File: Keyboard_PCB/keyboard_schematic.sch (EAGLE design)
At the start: 260 parts, among them M2 KEYSWITCH-RGBSMDLED-ALPSMX-1U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, M3 KEYSWITCH-RGBSMDLED-ALPSMX-1U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, M4 KEYSWITCH-RGBSMDLED-ALPSMX-1U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, M5 KEYSWITCH-RGBSMDLED-ALPSMX-1U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, M6 KEYSWITCH-RGBSMDLED-ALPSMX-1U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, Y2 CRYSTAL-GROUNDEDSMD-3.2X2.5

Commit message: Changed MCU to a larger chip
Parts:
- removed J1: (no value), SparkFun-Connectors:USB_MICRO-B_FEMALE-SMT
- removed U$1: 32U4, SparkFun-IC-Microcontroller:ATMEGA32U4TQFP-44
- added IC1: LMV321M5, linear:LMV321M5
- added IC2: (no value), controller-micro_atmel_jd:AT90USB-QFN
- added R5, R6: 5.1k, rcl:R-US_M0805
- added R7: 475, rcl:R-US_M0805
- added R8: 150, rcl:R-US_M0805
- added T1: BC846, transistor:BC846
- added U$2: PCB_USB_CDS_1, USB_pcb_connectors:PCB_USB_CDS_1
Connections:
- new net +5V: IC1.V+, IC2.AREF, IC2.AVCC, IC2.VCC, IC2.VCC@1, R7.2, T1.C, U$2.A4, U$2.A9, U$2.B4, U$2.B9
- new net CC1: R5.1, U$2.A5
- new net CC2: IC1.+IN, R6.2, U$2.B5
- new net LED_VCC: T1.E
- new net N$116: IC1.-IN, R7.1, R8.2
- new net N$117: IC1.OUT, T1.B
- net COL1: no longer U$1.PF7(ADC7)
- net COL10: no longer U$1.PC6
- net COL11: no longer U$1.PD7(ADC10)
- net COL12: no longer U$1.PE6
- net COL2: no longer U$1.PF6(ADC6)
- net COL3: no longer U$1.PF5(ADC5)
- net COL4: no longer U$1.PF4(ADC4)
- net COL5: no longer U$1.PF1(ADC1)
- net COL6: no longer U$1.PF0(ADC0)
- net COL7: no longer U$1.PD1(SDA)
- net COL8: no longer U$1.PD0(SCL)
- net COL9: no longer U$1.PD4(ADC8)
- net D+32U: now also IC2.D+; no longer U$1.D+
- net D+USB: now also U$2.A6; no longer J1.D+
- net D-32U4: now also IC2.D-; no longer U$1.D-
- net D-USB: now also U$2.A7; no longer J1.D-
- net GND: now also IC1.V-, IC2.AGND, IC2.GND, IC2.GND@1, IC2.UGND, R5.2, R6.1, R8.1, U$2.A1, U$2.A12, U$2.B1, U$2.B12; no longer J1.GND, J1.SHIELD, U$1.GND@15, U$1.GND@23, U$1.GND@35, U$1.GND@43, U$1.UGND
- net PE2: now also IC2.PE2_ALE_HWB; no longer U$1.PE2/!HWB
- net RESET: now also IC2./RESET; no longer U$1.!RESET
- net ROW1.1: no longer U$1.PB4(ADC11)
- net ROW1.2: no longer U$1.PB5(ADC12)
- net ROW2.1: no longer U$1.PB6(ADC13)
- net ROW2.2: no longer U$1.PB7
- net ROW3.1: no longer U$1.PD6(ADC9)
- net ROW3.2: no longer U$1.PC7
- net ROW4.1: no longer U$1.PB0(SS)
- net ROW4.2: no longer U$1.PB1(SCK)
- net ROW5.1: no longer U$1.PB2(MOSI)
- net ROW5.2: no longer U$1.PB3(MISO)
- net ROW6.1: no longer U$1.PD5
- net UCAP: now also IC2.UCAP; no longer U$1.UCAP
- net VCC: no longer J1.VBUS, U$1.AVCC@24, U$1.AVCC@44, U$1.UVCC, U$1.VCC@14, U$1.VCC@34
- net XTAL1: now also IC2.XTAL1; no longer U$1.XTAL1
- net XTAL2: now also IC2.XTAL2; no longer U$1.XTAL2

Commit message: Updated Schematics and boards
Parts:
- removed IC2: (no value), controller-micro_atmel_jd:AT90USB-QFN
- removed U$2: PCB_USB_CDS_1, USB_pcb_connectors:PCB_USB_CDS_1
- added IC3: (no value), controller-micro_atmel_jd:AT90USB-TQFP
- added J1: 1-2295018-2, 1-2295018-2:1-2295018-2
- T1: value BC846 -> (none); device transistor:BC846 -> transistor:-NPN-SOT23-EBC
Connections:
- removed net COL11: EQUAL2.P0, KP_9.P0, KP_ASTERISK.P0, KP_DASH.P0, NEXTSONG.P0, PAUSEPLAY.P0
- removed net ROW1.1: DF1.C, DF11.C, DF3.C, DF5.C, DF7.C, DF9.C, DM6.C, DNEXTSONG1.C, DPAUSE.C, DPAUSEPLAY.C, DSCROLLLOCK.C, DVOLUMEUP.C
- removed net ROW1.2: DBACKSONG.C, DESC.C, DF10.C, DF12.C, DF2.C, DF4.C, DF6.C, DF8.C, DLOCK.C, DNEXTSONG.C, DPRTSC.C, DVOLUMNEDOWN.C
- removed net ROW2.1: D1.C, D3.C, D5.C, D7.C, D9.C, DBACKSPACE.C, DDASH.C, DHOME.C, DKP_DASH.C, DKP_SLASH.C, DM5.C
- removed net ROW2.2: D0.C, D2.C, D4.C, D6.C, D8.C, DEQUAL.C, DGRAVE.C, DINSERT.C, DKP_ASTERISK.C, DNUMLOCK.C, DPGUP.C, DUNDERSCORE.C
- removed net ROW3.1: DBACKSLASH.C, DE.C, DEND.C, DEQUAL2.C, DKP_8.C, DLBRACKET.C, DM4.C, DO.C, DQ.C, DT.C, DU.C
- removed net ROW3.2: DDELETE.C, DI.C, DKP_5.C, DKP_7.C, DKP_9.C, DP.C, DPGDN.C, DR.C, DRBRACKET.C, DTAB.C, DW.C, DY.C
- removed net ROW4.1: DA.C, DCTRL2.C, DD.C, DG.C, DJ.C, DKP_4.C, DKP_6.C, DKP_62.C, DL.C, DM3.C, DQUOTE.C
- removed net ROW4.2: DCAPSLOCK.C, DENTER.C, DENTER2.C, DF.C, DH.C, DK.C, DKP_52.C, DS.C, DSEMICOLON.C, DUP.C
- removed net ROW5.1: DB.C, DC.C, DKP_2.C, DLEFT.C, DM.C, DM2.C, DMENU.C, DPERIOD.C, DZ.C
- removed net ROW5.2: DCOMMA.C, DDELETE2.C, DKP_1.C, DKP_3.C, DN.C, DRIGHT.C, DSHIFT.C, DSHIFT2.C, DSLASH.C, DV.C, DX.C
- removed net ROW6.1: DALT.C, DALT2.C, DBACKSPACE_1.C, DCTRL.C, DDOWN.C, DKP_0.C, DKP_DEL.C, DM1.C, DSPACE.C, DWIN.C, DWIN2.C
- new net COL13: 0.P0, F10.P0, P.P0, SEMICOLON.P0, SLASH.P0, WIN2.P0
- new net COL14: DASH.P0, F11.P0, LBRACKET.P0, MENU.P0, QUOTE.P0
- new net COL15: EQUAL.P0, F12.P0, RBRACKET.P0
- new net COL16: VOLUMEUP.P0
- new net COL17: BACKSLASH.P0, BACKSPACE.P0, CTRL2.P0, ENTER.P0, SHIFT2.P0, VOLUMNEDOWN.P0
- new net COL18: DELETE.P0, INSERT.P0, LEFT.P0, PRTSC.P0
- new net COL19: DOWN.P0, END.P0, HOME.P0, SCROLLLOCK.P0, UP.P0
- new net COL20: PAUSE.P0, PGDN.P0, PGUP.P0, RIGHT.P0
- new net COL21: BACKSONG.P0, KP_0.P0, KP_1.P0, KP_4.P0, KP_7.P0, NUMLOCK.P0
- new net COL22: KP_2.P0, KP_52.P0, KP_8.P0, KP_SLASH.P0, PAUSEPLAY.P0
- new net COL23: KP_3.P0, KP_6.P0, KP_9.P0, KP_ASTERISK.P0, KP_DEL.P0, NEXTSONG.P0
- new net COL24: ENTER2.P0, EQUAL2.P0, KP_DASH.P0, RANDSONG.P0
- new net COL25: BACKSPACE_1.P0, KP_5.P0, KP_62.P0, KP_DELETE2.P0, LOCK.P0, UNDERSCORE.P0
- new net LED1: M6.DI
- new net LED2: M5.DI
- new net LED3: M4.DI
- new net LED4: M3.DI
- new net LED5: M2.DI
- new net LED6: CTRL1.DI
- new net N$107: ESC.DI, M6.DO
- new net N$118: ESC.DO, F1.DI
- new net N$119: F1.DO, F2.DI
- new net N$121: F2.DO, F3.DI
- new net N$122: F3.DO, F4.DI
- new net N$123: F4.DO, F5.DI
- new net N$124: F5.DO, F6.DI
- new net N$132: F6.DO, F7.DI
- new net N$133: F7.DO, F8.DI
- new net N$134: F8.DO, F9.DI
- new net N$135: F10.DI, F9.DO
- new net N$136: F10.DO, F11.DI
- new net N$137: F11.DO, F12.DI
- new net N$138: F12.DO, VOLUMEUP.DI
- new net N$139: VOLUMEUP.DO, VOLUMNEDOWN.DI
- new net N$140: PRTSC.DI, VOLUMNEDOWN.DO
- new net N$141: PRTSC.DO, SCROLLLOCK.DI
- new net N$142: PAUSE.DI, SCROLLLOCK.DO
- new net N$143: BACKSONG.DI, PAUSE.DO
- new net N$144: BACKSONG.DO, PAUSEPLAY.DI
- new net N$145: NEXTSONG.DI, PAUSEPLAY.DO
- new net N$146: NEXTSONG.DO, RANDSONG.DI
- new net N$147: LOCK.DI, RANDSONG.DO
- new net N$148: IC3.PA1_AD1
- new net N$149: GRAVE.DI, M5.DO
- new net N$150: 1.DI, GRAVE.DO
- new net N$151: 1.DO, 2.DI
- new net N$152: 2.DO, 3.DI
- new net N$153: 3.DO, 4.DI
- new net N$154: 4.DO, 5.DI
- new net N$155: 5.DO, 6.DI
- new net N$156: 6.DO, 7.DI
- new net N$157: 7.DO, 8.DI
- new net N$158: 8.DO, 9.DI
- new net N$159: 0.DI, 9.DO
- new net N$160: 0.DO, DASH.DI
- new net N$161: DASH.DO, EQUAL.DI
- new net N$162: IC3.PA2_AD2
- new net N$163: BACKSPACE.DI, EQUAL.DO
- new net N$164: BACKSPACE.DO, INSERT.DI
- new net N$165: HOME.DI, INSERT.DO
- new net N$166: HOME.DO, PGUP.DI
- new net N$167: NUMLOCK.DI, PGUP.DO
- new net N$168: KP_SLASH.DI, NUMLOCK.DO
- new net N$169: KP_ASTERISK.DI, KP_SLASH.DO
- new net N$170: KP_ASTERISK.DO, KP_DASH.DI
- new net N$171: KP_DASH.DO, UNDERSCORE.DI
- new net N$172: M4.DO, TAB.DI
- new net N$173: Q.DI, TAB.DO
- new net N$174: Q.DO, W.DI
- new net N$175: E.DI, W.DO
- new net N$176: E.DO, R.DI
- new net N$177: R.DO, T.DI
- new net N$178: T.DO, Y.DI
- new net N$179: U.DI, Y.DO
- new net N$180: I.DI, U.DO
- new net N$181: I.DO, O.DI
- new net N$182: O.DO, P.DI
- new net N$183: LBRACKET.DI, P.DO
- new net N$184: LBRACKET.DO, RBRACKET.DI
- new net N$185: BACKSLASH.DI, RBRACKET.DO
- new net N$186: IC3.PA3_AD3
- new net N$187: BACKSLASH.DO, DELETE.DI
- new net N$188: DELETE.DO, END.DI
- new net N$189: END.DO, PGDN.DI
- new net N$190: KP_7.DI, PGDN.DO
- new net N$191: KP_7.DO, KP_8.DI
- new net N$192: KP_8.DO, KP_9.DI
- new net N$193: EQUAL2.DI, KP_9.DO
- new net N$194: EQUAL2.DO, KP_5.DI
- new net N$195: CAPSLOCK.DI, M3.DO
- new net N$196: A.DI, CAPSLOCK.DO
- new net N$197: A.DO, S.DI
- new net N$198: D.DI, S.DO
- new net N$199: D.DO, F.DI
- new net N$200: F.DO, G.DI
- new net N$201: G.DO, H.DI
- new net N$202: H.DO, J.DI
- new net N$203: J.DO, K.DI
- new net N$204: K.DO, L.DI
- new net N$205: L.DO, SEMICOLON.DI
- new net N$206: QUOTE.DI, SEMICOLON.DO
- new net N$207: ENTER.DI, QUOTE.DO
- new net N$208: ENTER.DO, KP_4.DI
- new net N$209: ENTER2.DI, KP_3.DO
- new net N$210: KP_4.DO, KP_52.DI
- new net N$211: KP_52.DO, KP_6.DI
- new net N$212: KP_6.DO, KP_62.DI
- new net N$213: IC3.PA4_AD4
- new net N$214: M2.DO, SHIFT.DI
- new net N$215: SHIFT.DO, Z.DI
- new net N$216: X.DI, Z.DO
- new net N$217: C.DI, X.DO
- new net N$218: C.DO, V.DI
- new net N$219: B.DI, V.DO
- new net N$220: B.DO, N.DI
- new net N$221: M.DI, N.DO
- new net N$222: COMMA.DI, M.DO
- new net N$223: COMMA.DO, PERIOD.DI
- new net N$224: PERIOD.DO, SLASH.DI
- new net N$225: SHIFT2.DI, SLASH.DO
- new net N$226: IC3.PA5_AD5
- new net N$227: KP_1.DO, KP_2.DI
- new net N$228: KP_2.DO, KP_3.DI
- new net N$229: ENTER2.DO, KP_DELETE2.DI
- new net N$230: KP_1.DI, SHIFT2.DO
- new net N$231: IC3.PA6_AD6
- new net N$232: CTRL.DI, CTRL1.DO
- new net N$233: CTRL.DO, WIN.DI
- new net N$234: ALT.DI, WIN.DO
- new net N$235: ALT.DO, SPACE.DI
- new net N$236: IC3.PA7_AD7
- new net N$238: ALT2.DI, SPACE.DO
- new net N$239: J1.VBUS@4
- new net N$242: ALT2.DO, WIN2.DI
- new net N$243: MENU.DI, WIN2.DO
- new net N$245: CTRL2.DI, MENU.DO
- new net N$246: CTRL2.DO, LEFT.DI
- new net N$247: KP_0.DI
- new net N$248: KP_0.DO, KP_DEL.DI
- new net N$249: BACKSPACE_1.DI, KP_DEL.DO
- new net N$250: DOWN.DI, LEFT.DO
- new net N$251: DOWN.DO, RIGHT.DI
- new net N$252: RIGHT.DO
- new net ROW1: DBACKSONG.C, DESC.C, DF1.C, DF10.C, DF11.C, DF12.C, DF2.C, DF3.C, DF4.C, DF5.C, DF6.C, DF7.C, DF8.C, DF9.C, DLOCK.C, DM6.C, DNEXTSONG.C, DNEXTSONG1.C, DPAUSE.C, DPAUSEPLAY.C, DPRTSC.C, DSCROLLLOCK.C, DVOLUMEUP.C, DVOLUMNEDOWN.C
- new net ROW2: D0.C, D1.C, D2.C, D3.C, D4.C, D5.C, D6.C, D7.C, D8.C, D9.C, DBACKSPACE.C, DDASH.C, DEQUAL.C, DGRAVE.C, DHOME.C, DINSERT.C, DKP_ASTERISK.C, DKP_DASH.C, DKP_SLASH.C, DM5.C, DNUMLOCK.C, DPGUP.C, DUNDERSCORE.C
- new net ROW3: DBACKSLASH.C, DDELETE.C, DE.C, DEND.C, DEQUAL2.C, DI.C, DKP_5.C, DKP_7.C, DKP_8.C, DKP_9.C, DLBRACKET.C, DM4.C, DO.C, DP.C, DPGDN.C, DQ.C, DR.C, DRBRACKET.C, DT.C, DTAB.C, DU.C, DW.C, DY.C
- new net ROW4: DA.C, DCAPSLOCK.C, DD.C, DENTER.C, DF.C, DG.C, DH.C, DJ.C, DK.C, DKP_4.C, DKP_52.C, DKP_6.C, DKP_62.C, DL.C, DM3.C, DQUOTE.C, DS.C, DSEMICOLON.C
- new net ROW5: DB.C, DC.C, DCOMMA.C, DDELETE2.C, DENTER2.C, DKP_1.C, DKP_2.C, DKP_3.C, DM.C, DM2.C, DN.C, DPERIOD.C, DSHIFT.C, DSHIFT2.C, DSLASH.C, DUP.C, DV.C, DX.C, DZ.C
- new net ROW6: DALT.C, DALT2.C, DBACKSPACE_1.C, DCTRL2.C, DDOWN.C, DKP_0.C, DKP_DEL.C, DLEFT.C, DM1.C, DMENU.C, DRIGHT.C, DSPACE.C, DWIN.C, DWIN2.C
- net +5V: now also IC3.AREF, IC3.AVCC, IC3.VCC, IC3.VCC@1, J1.VBUS@1, J1.VBUS@2, J1.VBUS@3; no longer IC2.AREF, IC2.AVCC, IC2.VCC, IC2.VCC@1, U$2.A4, U$2.A9, U$2.B4, U$2.B9
- net CC1: now also IC1.+IN, J1.CC1, R6.2; no longer R5.1, U$2.A5
- net CC2: now also J1.CC2, R5.1; no longer IC1.+IN, R6.2, U$2.B5
- net COL1: no longer CAPSLOCK.P0, ESC.P0, GRAVE.P0, SHIFT.P0, TAB.P0
- net COL10: now also 8.P0, COMMA.P0, F8.P0, I.P0, K.P0; no longer BACKSONG.P0, ENTER2.P0, KP_3.P0, KP_6.P0, KP_7.P0, KP_8.P0, KP_DEL.P0, KP_SLASH.P0, NUMLOCK.P0, PAUSE.P0
- net COL12: now also 9.P0, ALT2.P0, F9.P0, L.P0, O.P0, PERIOD.P0; no longer BACKSPACE_1.P0, KP_5.P0, KP_62.P0, KP_DELETE2.P0, LOCK.P0, RANDSONG.P0, UNDERSCORE.P0
- net COL2: now also CAPSLOCK.P0, ESC.P0, GRAVE.P0, SHIFT.P0, TAB.P0; no longer 1.P0, 2.P0, A.P0, F1.P0, F2.P0, Q.P0, S.P0, W.P0, X.P0, Z.P0
- net COL3: now also 1.P0, A.P0, F1.P0, Q.P0, Z.P0; no longer 3.P0, 4.P0, C.P0, D.P0, E.P0, F.P0, F3.P0, F4.P0, R.P0, V.P0
- net COL4: now also 2.P0, F2.P0, S.P0, W.P0, X.P0; no longer 5.P0, 6.P0, B.P0, F5.P0, F6.P0, G.P0, H.P0, N.P0, T.P0, Y.P0
- net COL5: now also 3.P0, C.P0, D.P0, E.P0, F3.P0; no longer 7.P0, 8.P0, COMMA.P0, F7.P0, F8.P0, I.P0, J.P0, K.P0, M.P0, SPACE.P0, U.P0
- net COL6: now also 4.P0, F.P0, F4.P0, R.P0, V.P0; no longer 0.P0, 9.P0, ALT2.P0, F10.P0, F9.P0, L.P0, O.P0, P.P0, PERIOD.P0, SEMICOLON.P0, SLASH.P0
- net COL7: now also 5.P0, B.P0, F5.P0, G.P0, SPACE.P0, T.P0; no longer DASH.P0, ENTER.P0, EQUAL.P0, F11.P0, F12.P0, LBRACKET.P0, MENU.P0, QUOTE.P0, RBRACKET.P0, SHIFT2.P0, WIN2.P0
- net COL8: now also 6.P0, F6.P0, H.P0, N.P0, Y.P0; no longer BACKSLASH.P0, BACKSPACE.P0, CTRL2.P0, DELETE.P0, DOWN.P0, INSERT.P0, LEFT.P0, RIGHT.P0, UP.P0, VOLUMEUP.P0, VOLUMNEDOWN.P0
- net COL9: now also 7.P0, F7.P0, J.P0, M.P0, U.P0; no longer END.P0, HOME.P0, KP_0.P0, KP_1.P0, KP_2.P0, KP_4.P0, KP_52.P0, PGDN.P0, PGUP.P0, PRTSC.P0, SCROLLLOCK.P0
- net D+32U: now also IC3.D+; no longer IC2.D+
- net D+USB: now also J1.D+@1; no longer U$2.A6
- net D-32U4: now also IC3.D-; no longer IC2.D-
- net D-USB: now also J1.D-@1; no longer U$2.A7
- net GND: now also IC3.AGND, IC3.GND, IC3.GND@1, IC3.UGND, J1.GND@1, J1.GND@2, J1.GND@3, J1.GND@4, J1.SHIELD; no longer IC2.AGND, IC2.GND, IC2.GND@1, IC2.UGND, U$2.A1, U$2.A12, U$2.B1, U$2.B12
- net N$102: now also IC3.PA0_AD0; no longer CTRL.P1, DCTRL.A
- net PE2: now also IC3.PE2_ALE_HWB; no longer IC2.PE2_ALE_HWB
- net RESET: now also IC3./RESET; no longer IC2./RESET
- net UCAP: now also IC3.UCAP; no longer IC2.UCAP
- net XTAL1: now also IC3.XTAL1; no longer IC2.XTAL1
- net XTAL2: now also IC3.XTAL2; no longer IC2.XTAL2
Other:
- moved on the sheet: 1, A, ALT, ALT2, B, BACKSLASH, BACKSPACE, C, COMMA, CTRL2, D, D0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

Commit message: Updated board
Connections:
- net +5V: now also C3.1, C4.1, C5.1, C6.1, C7.1
- net VCC: no longer C3.1, C4.1, C5.1, C6.1, C7.1
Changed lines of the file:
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@@
 <net name="VCC" class="0">
-<segment>
-<pinref part="C3" gate="G$1" pin="1"/>
-<wire x1="-137.16" y1="154.94" x2="-137.16" y2="157.48" width="0.1524" layer="91"/>
-<wire x1="-137.16" y1="157.48" x2="-129.54" y2="157.48" width="0.1524" layer="91"/>
-<pinref part="C7" gate="G$1" pin="1"/>
-<wire x1="-129.54" y1="157.48" x2="-121.92" y2="157.48" width="0.1524" layer="91"/>
-<wire x1="-121.92" y1="157.48" x2="-114.3" y2="157.48" width="0.1524" layer="91"/>
-<wire x1="-114.3" y1="157.48" x2="-106.68" y2="157.48" width="0.1524" layer="91"/>
-<wire x1="-106.68" y1="157.48" x2="-106.68" y2="154.94" width="0.1524" layer="91"/>
-<pinref part="C6" gate="G$1" pin="1"/>
-<wire x1="-114.3" y1="154.94" x2="-114.3" y2="157.48" width="0.1524" layer="91"/>
-<junction x="-114.3" y="157.48"/>
-<pinref part="C5" gate="G$1" pin="1"/>
-<wire x1="-121.92" y1="154.94" x2="-121.92" y2="157.48" width="0.1524" layer="91"/>
-<junction x="-121.92" y="157.48"/>
-<pinref part="C4" gate="G$1" pin="1"/>
-<wire x1="-129.54" y1="154.94" x2="-129.54" y2="157.48" width="0.1524" layer="91"/>
-<junction x="-129.54" y="157.48"/>
-<wire x1="-137.16" y1="157.48" x2="-137.16" y2="160.02" width="0.1524" layer="91"/>
-<junction x="-137.16" y="157.48"/>
-<pinref part="P+1" gate="1" pin="+5V"/>
-</segment>
 <segment>
 <pinref part="P+2" gate="1" pin="+5V"/>
@@
 <pinref part="P+7" gate="1" pin="+5V"/>
 </segment>
+<segment>
+<pinref part="C3" gate="G$1" pin="1"/>
+<wire x1="-137.16" y1="154.94" x2="-137.16" y2="157.48" width="0.1524" layer="91"/>
+<wire x1="-137.16" y1="157.48" x2="-129.54" y2="157.48" width="0.1524" layer="91"/>
+<pinref part="C7" gate="G$1" pin="1"/>
+<wire x1="-129.54" y1="157.48" x2="-121.92" y2="157.48" width="0.1524" layer="91"/>
+<wire x1="-121.92" y1="157.48" x2="-114.3" y2="157.48" width="0.1524" layer="91"/>
+<wire x1="-114.3" y1="157.48" x2="-106.68" y2="157.48" width="0.1524" layer="91"/>
+<wire x1="-106.68" y1="157.48" x2="-106.68" y2="154.94" width="0.1524" layer="91"/>
+<pinref part="C6" gate="G$1" pin="1"/>
+<wire x1="-114.3" y1="154.94" x2="-114.3" y2="157.48" width="0.1524" layer="91"/>
+<junction x="-114.3" y="157.48"/>
+<pinref part="C5" gate="G$1" pin="1"/>
+<wire x1="-121.92" y1="154.94" x2="-121.92" y2="157.48" width="0.1524" layer="91"/>
+<junction x="-121.92" y="157.48"/>
+<pinref part="C4" gate="G$1" pin="1"/>
+<wire x1="-129.54" y1="154.94" x2="-129.54" y2="157.48" width="0.1524" layer="91"/>
+<junction x="-129.54" y="157.48"/>
+<wire x1="-137.16" y1="157.48" x2="-137.16" y2="160.02" width="0.1524" layer="91"/>
+<junction x="-137.16" y="157.48"/>
+<pinref part="P+1" gate="1" pin="+5V"/>
+<label x="-134.62" y="157.48" size="1.778" layer="95"/>
+</segment>
 </net>

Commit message: Updated Board
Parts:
- removed IC1: LMV321M5, linear:LMV321M5
- removed R7: 475, rcl:R-US_M0805
- removed R8: 150, rcl:R-US_M0805
- removed T1: (no value), transistor:-NPN-SOT23-EBC
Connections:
- removed net CC1: IC1.+IN, J1.CC1, R6.2
- removed net CC2: J1.CC2, R5.1
- removed net LED_VCC: T1.E
- removed net N$102: IC3.PA0_AD0
- removed net N$116: IC1.-IN, R7.1, R8.2
- removed net N$117: IC1.OUT, T1.B
- removed net N$148: IC3.PA1_AD1
- removed net N$162: IC3.PA2_AD2
- removed net N$186: IC3.PA3_AD3
- removed net N$213: IC3.PA4_AD4
- removed net N$226: IC3.PA5_AD5
- removed net N$231: IC3.PA6_AD6
- removed net N$236: IC3.PA7_AD7
- removed net VCC: R1.1
- new net N$237: J1.CC1, R5.1
- new net N$255: J1.CC2, R6.2
- net +5V: now also IC3.UVCC, IC3.VBUS, J1.VBUS@4, R1.1; no longer IC1.V+, J1.VBUS@2, R7.2, T1.C
- net D+USB: now also J1.D+; no longer J1.D+@1
- net D-USB: now also J1.D-; no longer J1.D-@1
- net GND: no longer IC1.V-, R8.1
- net N$239: now also J1.VBUS@2; no longer J1.VBUS@4
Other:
- moved on the sheet: J1

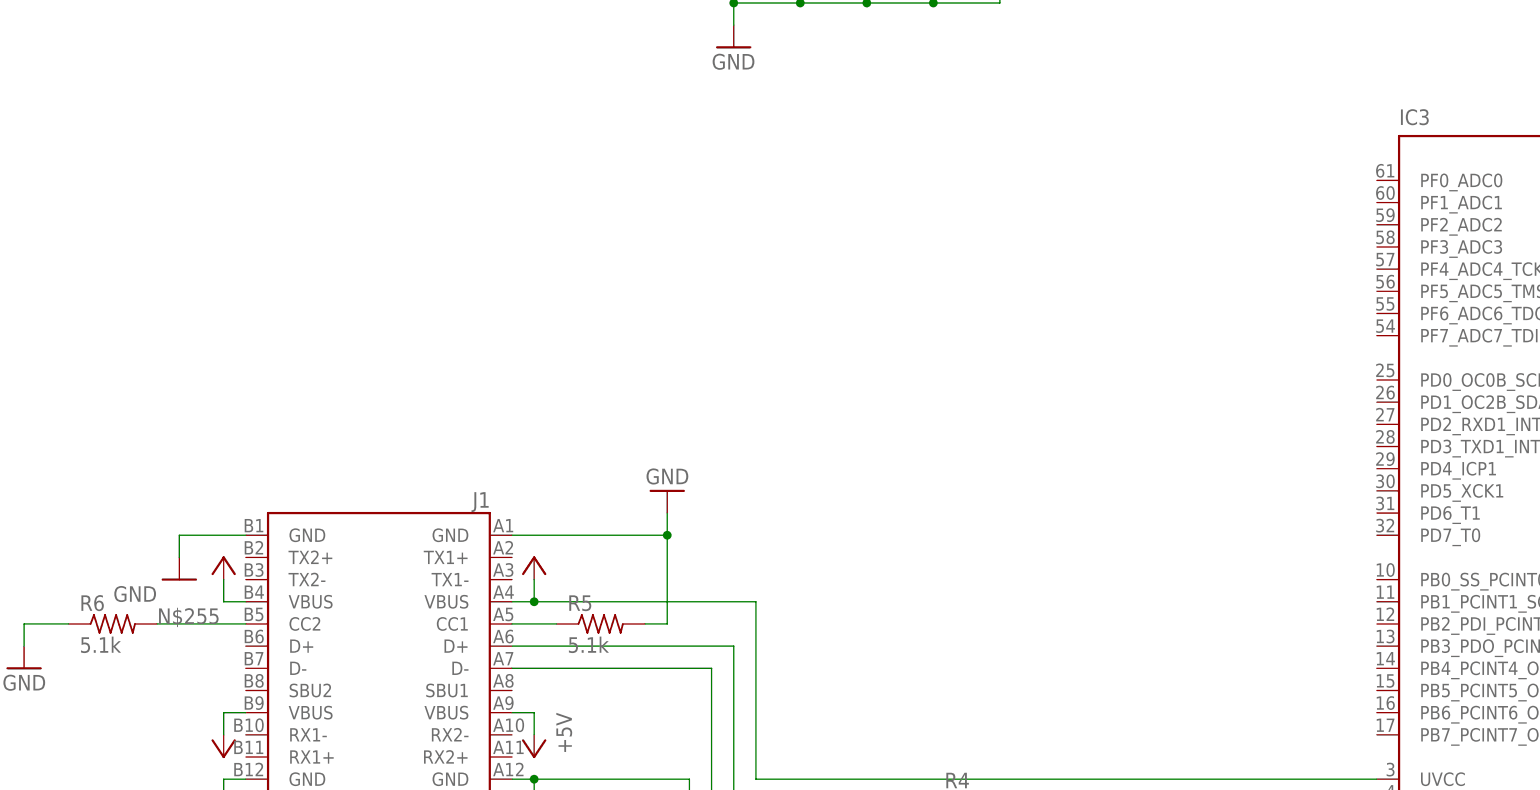
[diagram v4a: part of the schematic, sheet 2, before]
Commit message: Updated Schematic and rerouted board
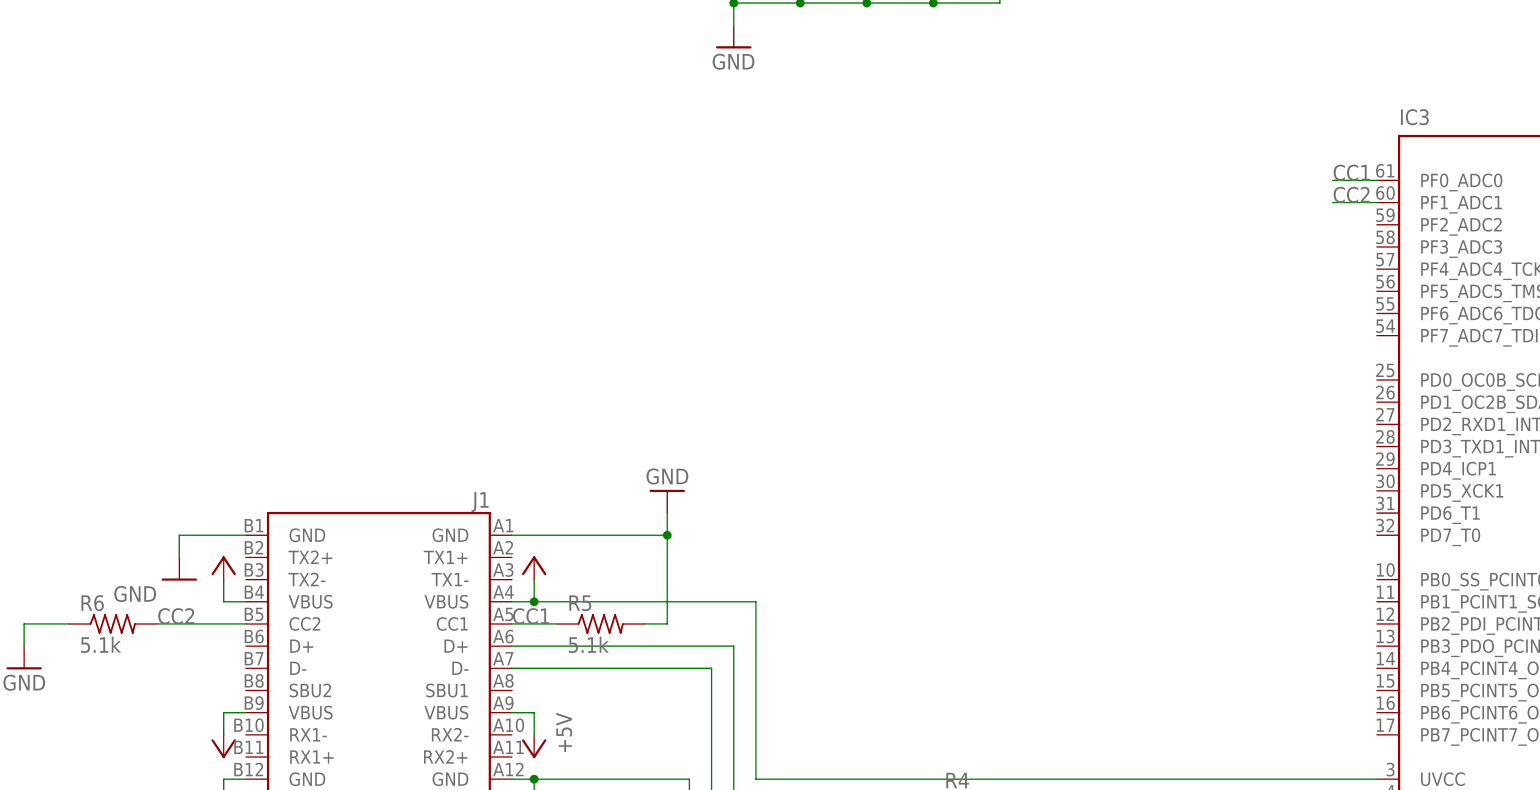
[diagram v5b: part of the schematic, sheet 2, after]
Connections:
- removed net N$237: J1.CC1, R5.1
- removed net N$255: J1.CC2, R6.2
- new net CC1: IC3.PF0_ADC0, J1.CC1, R5.1
- new net CC2: IC3.PF1_ADC1, J1.CC2, R6.2
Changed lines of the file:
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@@
 </segment>
 </net>
-<net name="N$237" class="0">
+<net name="CC1" class="0">
+<segment>
+<pinref part="IC3" gate="G$1" pin="PF0_ADC0"/>
+<wire x1="-63.5" y1="124.46" x2="-68.58" y2="124.46" width="0.1524" layer="91"/>
+<label x="-68.58" y="124.46" size="1.778" layer="95"/>
+</segment>
 <segment>
 <pinref part="R5" gate="G$1" pin="1"/>
 <pinref part="J1" gate="G$1" pin="CC1"/>
 <wire x1="-157.48" y1="73.66" x2="-162.56" y2="73.66" width="0.1524" layer="91"/>
+<label x="-162.56" y="73.66" size="1.778" layer="95"/>
 </segment>
 </net>
-<net name="N$255" class="0">
+<net name="CC2" class="0">
+<segment>
+<pinref part="IC3" gate="G$1" pin="PF1_ADC1"/>
+<wire x1="-63.5" y1="121.92" x2="-68.58" y2="121.92" width="0.1524" layer="91"/>
+<label x="-68.58" y="121.92" size="1.778" layer="95"/>
+</segment>
 <segment>
 <pinref part="J1" gate="G$1" pin="CC2"/>
